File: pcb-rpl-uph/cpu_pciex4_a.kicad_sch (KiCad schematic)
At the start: 1 part, among them U5 RPL_UPH_FCBGA1744

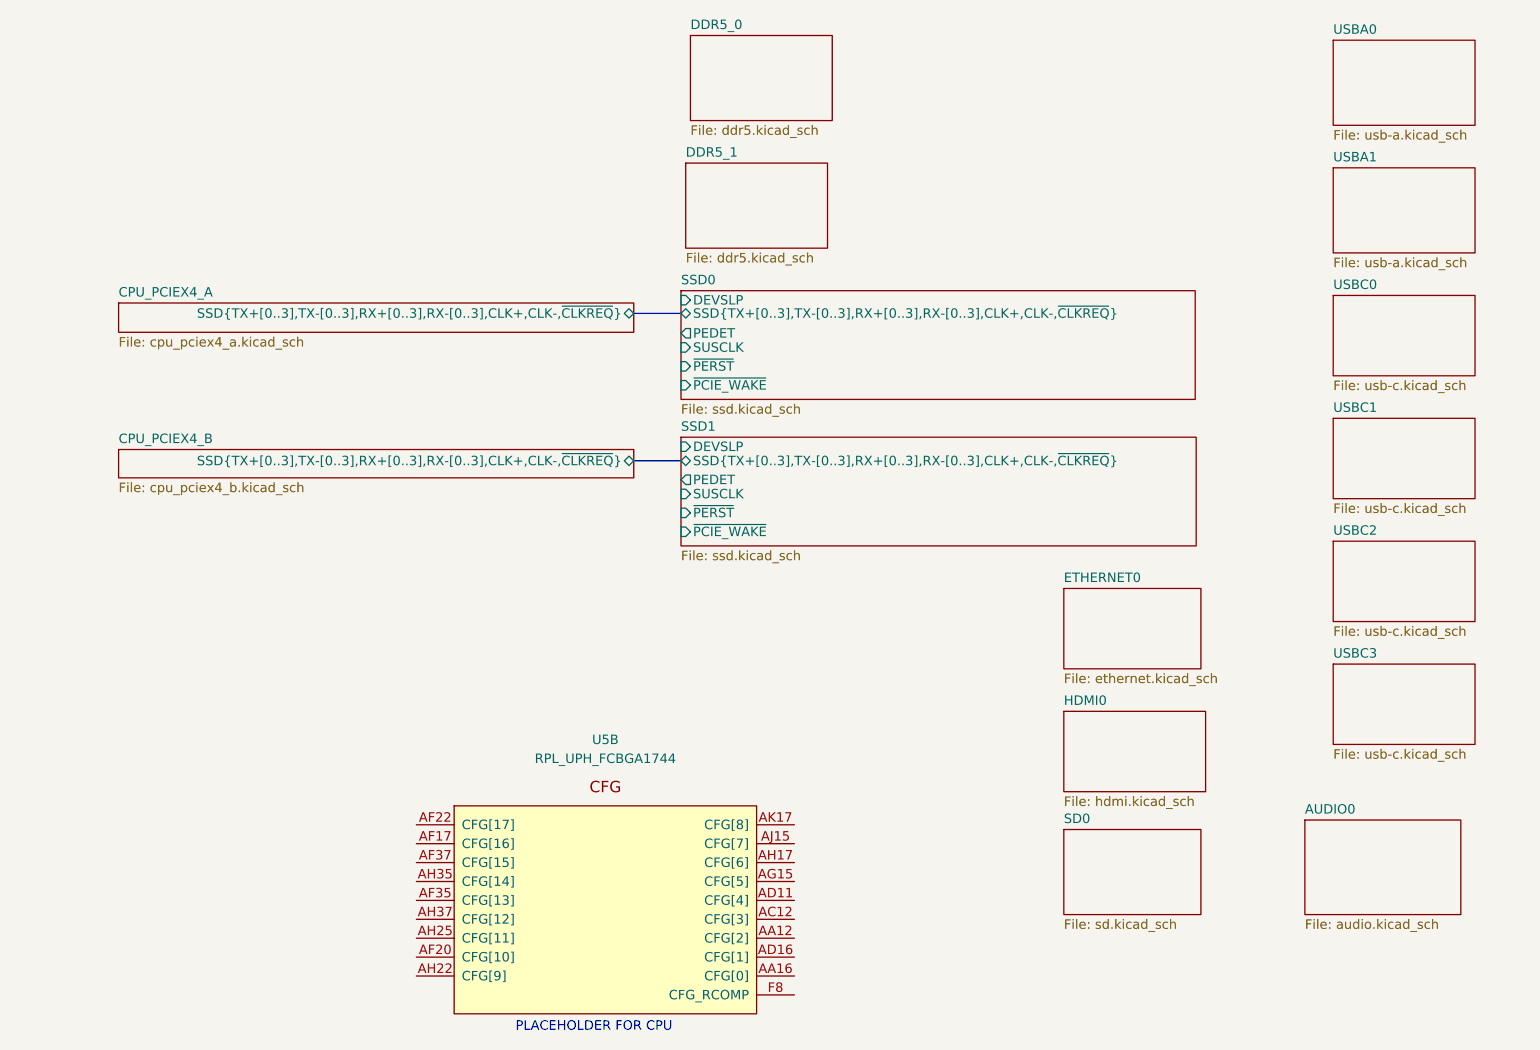
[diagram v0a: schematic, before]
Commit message: Connect SSD data signals
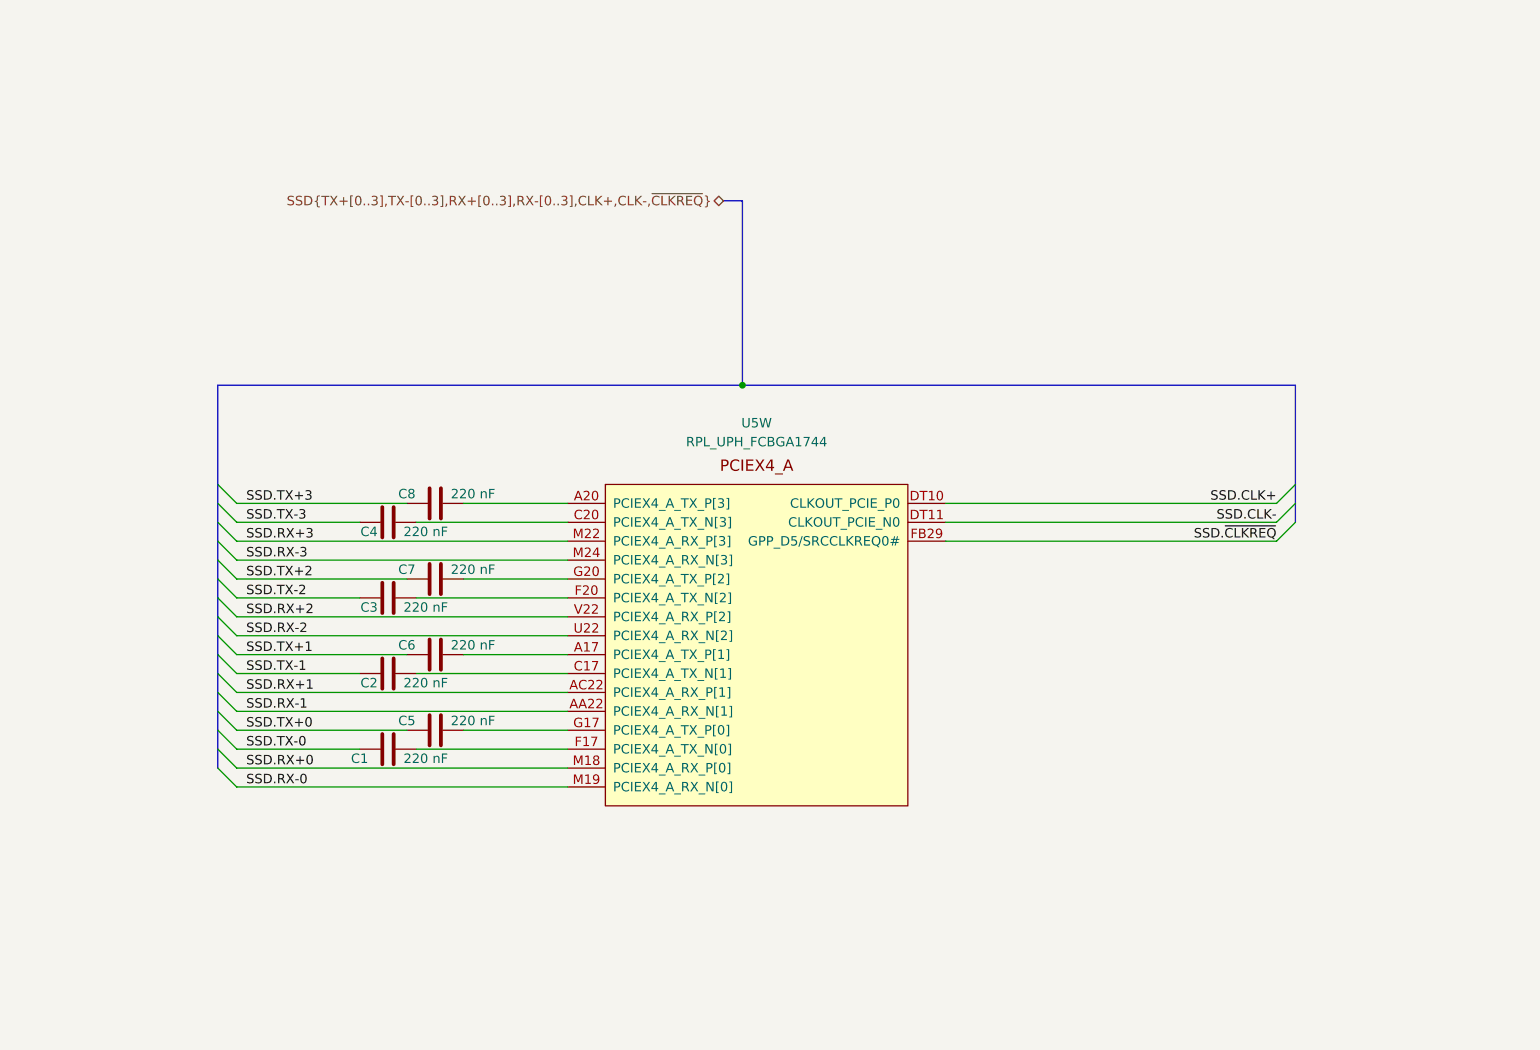
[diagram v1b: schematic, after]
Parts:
- removed U5: RPL_UPH_FCBGA1744, local:RPL_UPH_FCBGA1744, symbol local:RPL_UPH_FCBGA1744
- added C1, C2, C3, C4, C5, C6, C7, C8: 220 nF, local:C_0201_0603Metric, symbol Device:C
- added U5: RPL_UPH_FCBGA1744, symbol local:RPL_UPH_FCBGA1744
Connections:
- new net: C5.2, U5.G17 (PCIEX4_A_TX_P[0])
- new net: C7.2, U5.G20 (PCIEX4_A_TX_P[2])
- new net: C8.2, U5.A20 (PCIEX4_A_TX_P[3])
- new net: C6.2, U5.A17 (PCIEX4_A_TX_P[1])
- new net: C2.2, U5.C17 (PCIEX4_A_TX_N[1])
- new net: C4.2, U5.C20 (PCIEX4_A_TX_N[3])
- new net: C1.2, U5.F17 (PCIEX4_A_TX_N[0])
- new net: C3.2, U5.F20 (PCIEX4_A_TX_N[2])
- new net SSD.CLK+: U5.DT10 (CLKOUT_PCIE_P0)
- new net SSD.CLK-: U5.DT11 (CLKOUT_PCIE_N0)
- new net SSD.RX+0: U5.M18 (PCIEX4_A_RX_P[0])
- new net SSD.RX+1: U5.AC22 (PCIEX4_A_RX_P[1])
- new net SSD.RX+2: U5.V22 (PCIEX4_A_RX_P[2])
- new net SSD.RX+3: U5.M22 (PCIEX4_A_RX_P[3])
- new net SSD.RX-0: U5.M19 (PCIEX4_A_RX_N[0])
- new net SSD.RX-1: U5.AA22 (PCIEX4_A_RX_N[1])
- new net SSD.RX-2: U5.U22 (PCIEX4_A_RX_N[2])
- new net SSD.RX-3: U5.M24 (PCIEX4_A_RX_N[3])
- new net SSD.TX+0: C5.1
- new net SSD.TX+1: C6.1
- new net SSD.TX+2: C7.1
- new net SSD.TX+3: C8.1
- new net SSD.TX-0: C1.1
- new net SSD.TX-1: C2.1
- new net SSD.TX-2: C3.1
- new net SSD.TX-3: C4.1
- new net SSD.~{CLKREQ}: U5.FB29 (GPP_D5/SRCCLKREQ0#)
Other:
- removed sheet AUDIO0
- removed sheet CPU_PCIEX4_A
- removed sheet CPU_PCIEX4_B
- removed sheet DDR5_0
- removed sheet DDR5_1
- removed sheet ETHERNET0
- removed sheet HDMI0
- removed sheet SD0
- removed sheet SSD0
- removed sheet SSD1
- removed sheet USBA0
- removed sheet USBA1
- removed sheet USBC0
- removed sheet USBC1
- removed sheet USBC2
- removed sheet USBC3
- note removed: "PLACEHOLDER FOR CPU"

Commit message: Remove extra DC block caps on M.2 PCIe signals
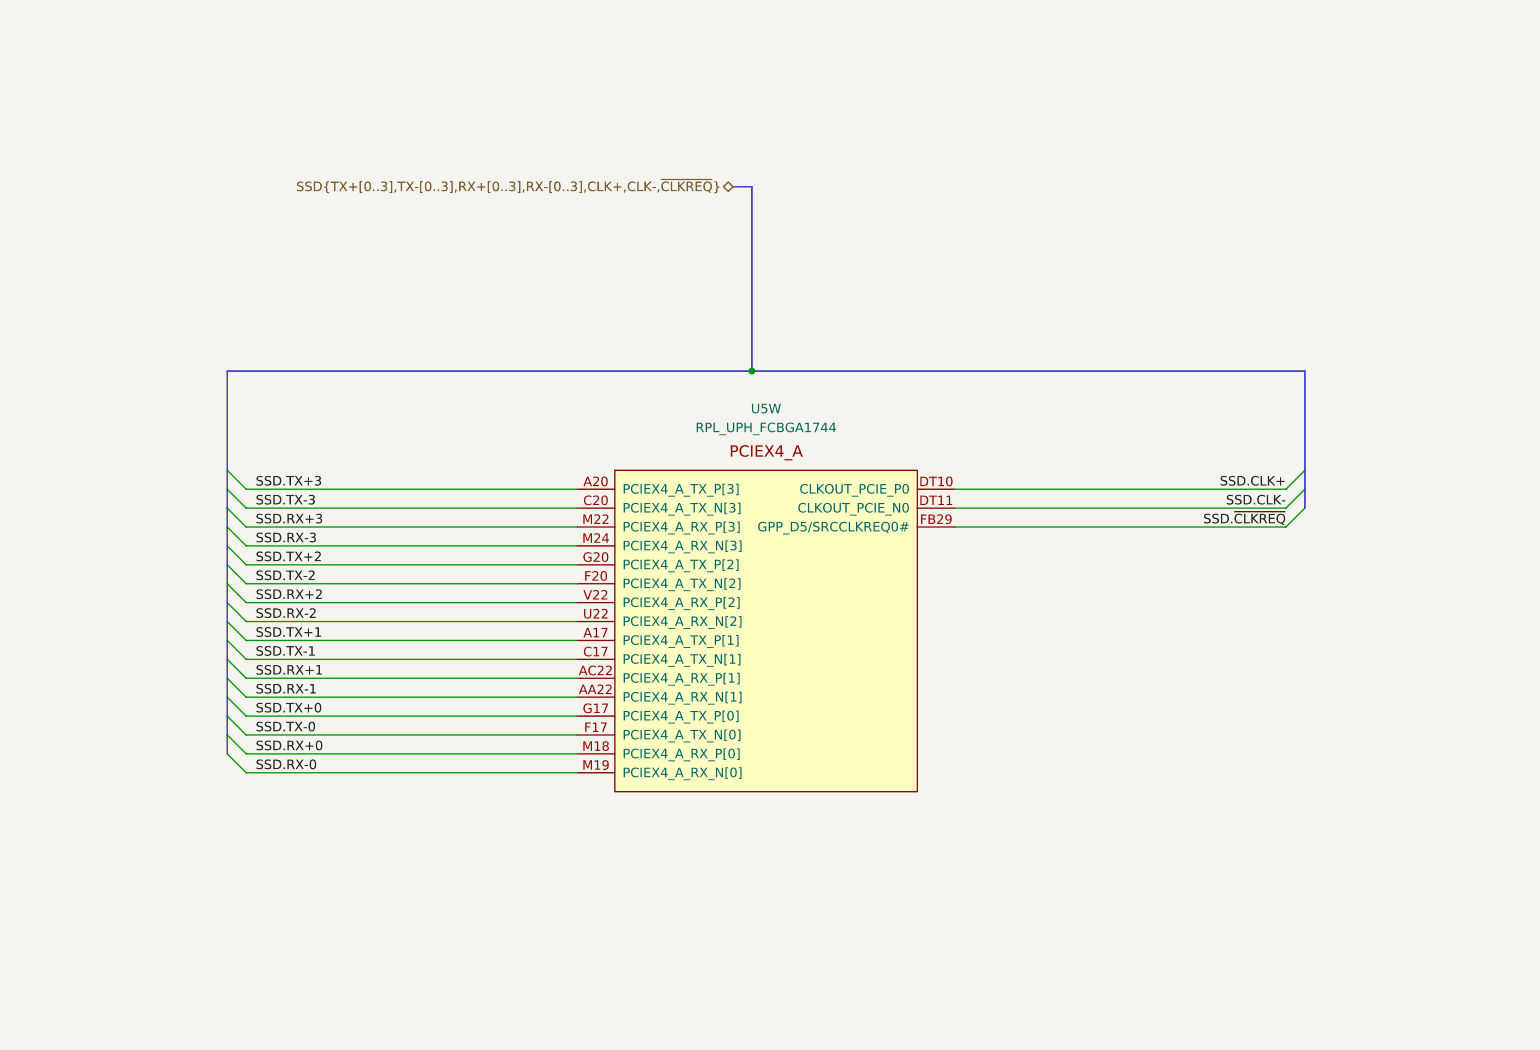
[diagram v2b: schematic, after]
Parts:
- removed C1, C2, C3, C4, C5, C6, C7, C8: 220 nF, local:C_0201_0603Metric, symbol Device:C
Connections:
- net SSD.TX+0: now also U5.G17 (PCIEX4_A_TX_P[0])
- net SSD.TX+1: now also U5.A17 (PCIEX4_A_TX_P[1])
- net SSD.TX+2: now also U5.G20 (PCIEX4_A_TX_P[2])
- net SSD.TX+3: now also U5.A20 (PCIEX4_A_TX_P[3])
- net SSD.TX-0: now also U5.F17 (PCIEX4_A_TX_N[0])
- net SSD.TX-1: now also U5.C17 (PCIEX4_A_TX_N[1])
- net SSD.TX-2: now also U5.F20 (PCIEX4_A_TX_N[2])
- net SSD.TX-3: now also U5.C20 (PCIEX4_A_TX_N[3])
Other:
- moved on the sheet: U5W

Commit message: add display connector
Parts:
- U5: footprint (none) -> local:RPL_UPH_FCBGA1744
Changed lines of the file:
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@@
       (effects (font (size 1.27 1.27)))
     )
-    (property "Footprint" "" (at 153.67 69.85 0)
+    (property "Footprint" "local:RPL_UPH_FCBGA1744" (at 153.67 69.85 0)
       (effects (font (size 1.27 1.27)) hide)
     )
